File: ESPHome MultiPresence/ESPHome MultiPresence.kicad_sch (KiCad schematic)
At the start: 20 parts

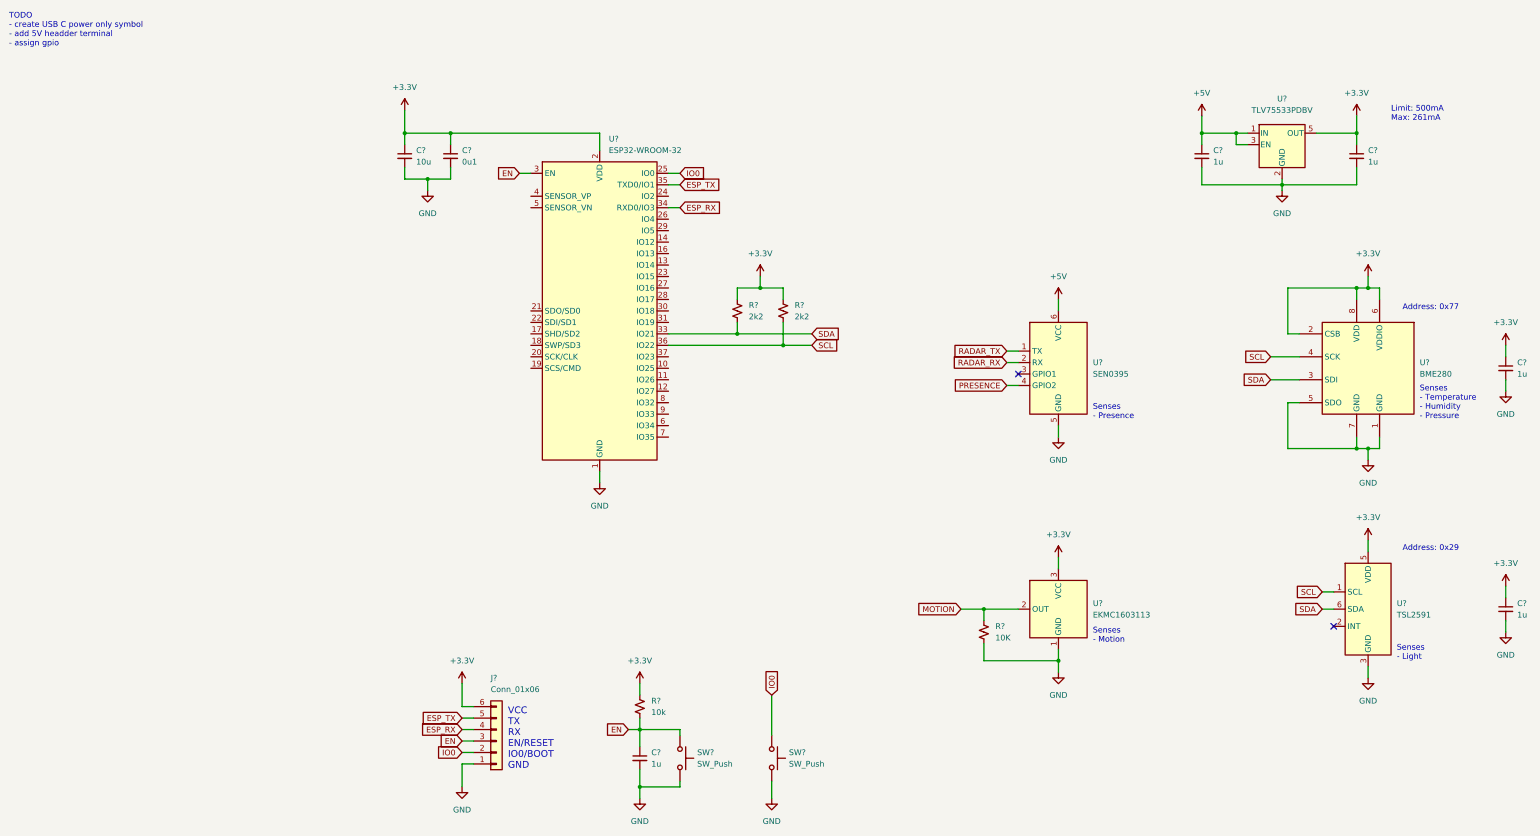
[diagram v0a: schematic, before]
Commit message: split schematic into 2 sheets, assigned all but J3 and SW3 footprints, started pcb layout
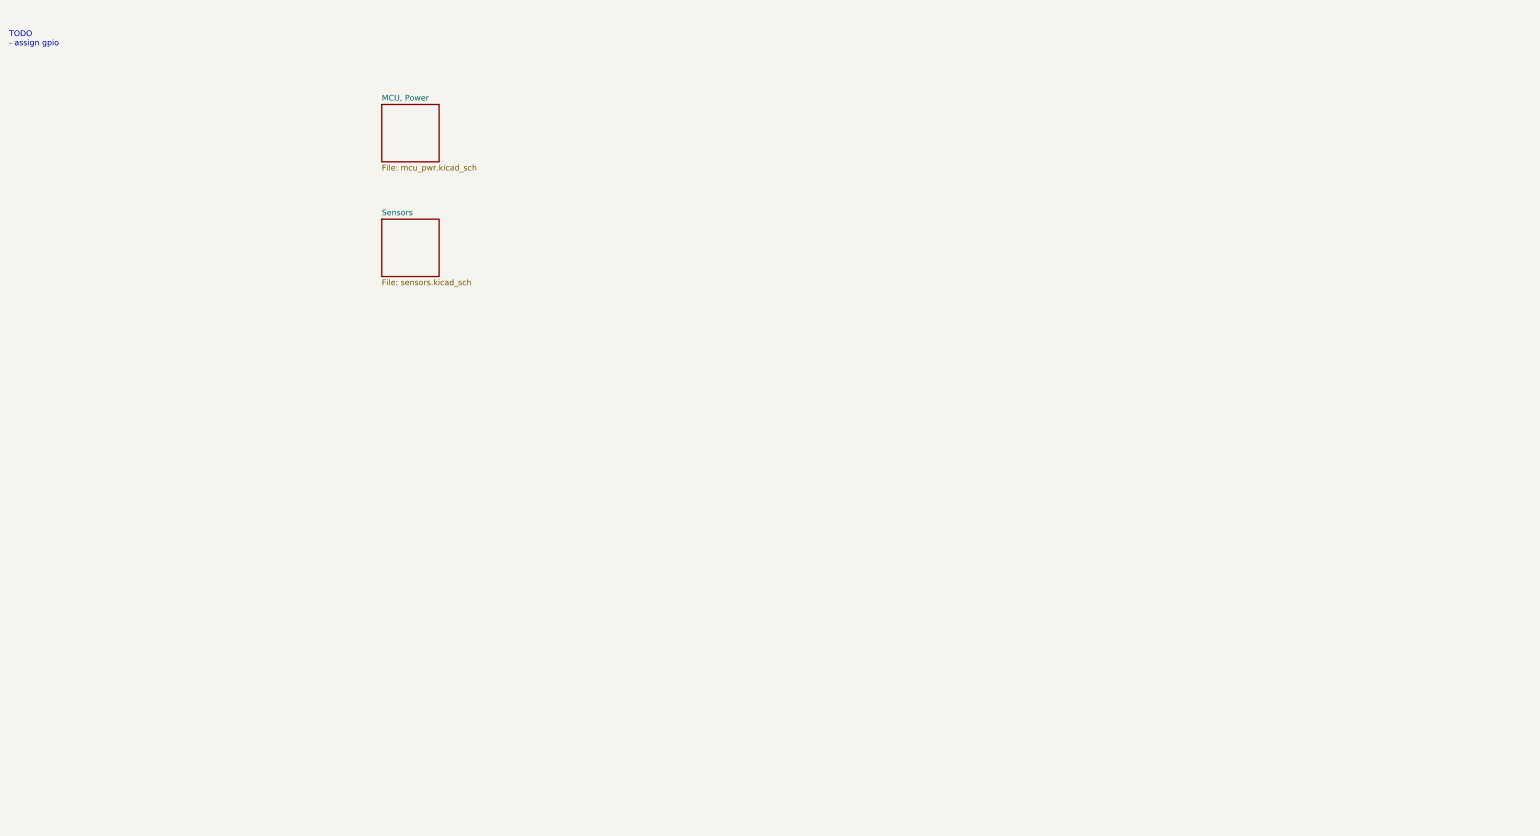
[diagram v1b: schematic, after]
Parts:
- removed C? (x5): 1u, symbol Device:C_Small
- removed C?: 0u1, symbol Device:C_Small
- removed C?: 10u, symbol Device:C_Small
- removed J?: Conn_01x06, symbol Connector_Generic:Conn_01x06
- removed R? (x2): 2k2, symbol Device:R_Small_US
- removed R?: 10k, symbol Device:R_Small_US
- removed R?: 10K, symbol Device:R_Small_US
- removed SW? (x2): SW_Push, symbol Switch:SW_Push
- removed U?: EKMC1603113, symbol My Symbols:EKMxxxxxxxxx
- removed U?: ESP32-WROOM-32, RF_Module:ESP32-WROOM-32, symbol RF_Module:ESP32-WROOM-32
- removed U?: TSL2591, symbol My Symbols:TSL2591
- removed U?: SEN0395, symbol My Symbols:SEN0395
- removed U?: BME280, Package_LGA:Bosch_LGA-8_2.5x2.5mm_P0.65mm_ClockwisePinNumbering, symbol Sensor:BME280
- removed U?: TLV75533PDBV, Package_TO_SOT_SMD:SOT-23-5, symbol Regulator_Linear:TLV75533PDBV
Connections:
- no-connect marks 2 -> 0
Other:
- added sheet MCU, Power (mcu_pwr.kicad_sch)
- added sheet Sensors (sensors.kicad_sch)
- note added: "TODO - assign gpio"
- note removed: "Address: 0x29"
- note removed: "Address: 0x77"
- note removed: "Limit: 500mA Max: 261mA"
- note removed: "Senses - Light"
- note removed: "Senses - Motion"
- note removed: "Senses - Presence"
- note removed: "Senses - Temperature - Humidity - Pressure"
- note removed: "TODO - create USB C power only symbol - add 5V headder terminal - assign gpio"
- note removed: "VCC TX RX EN/RESET IO0/BOOT GND"
- title: (none) -> ESPHome MultiPresence Sensor
